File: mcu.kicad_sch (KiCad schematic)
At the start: 33 parts, among them J3 Conn_ARM_SWD_TagConnect_TC203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, J4 Conn_01x02_Pin, U7 RP2040, U9 AT25xxx, Y1 830070868

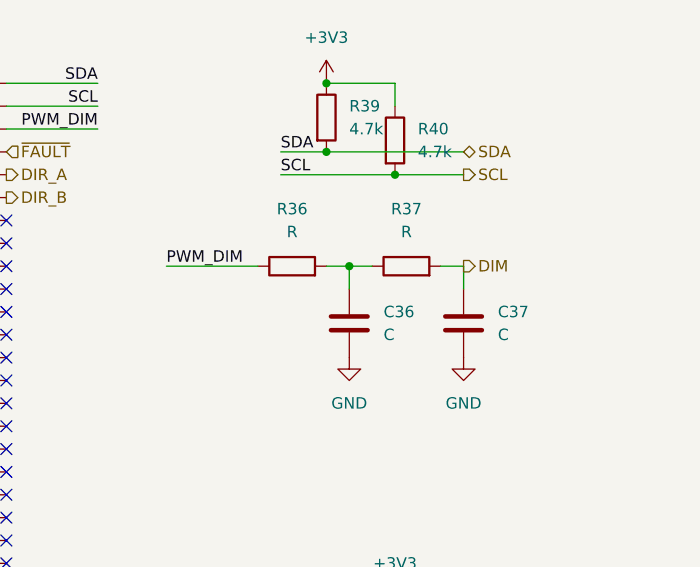
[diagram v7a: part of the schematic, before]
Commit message: Filter values
Updated filter component values from lab experimentation
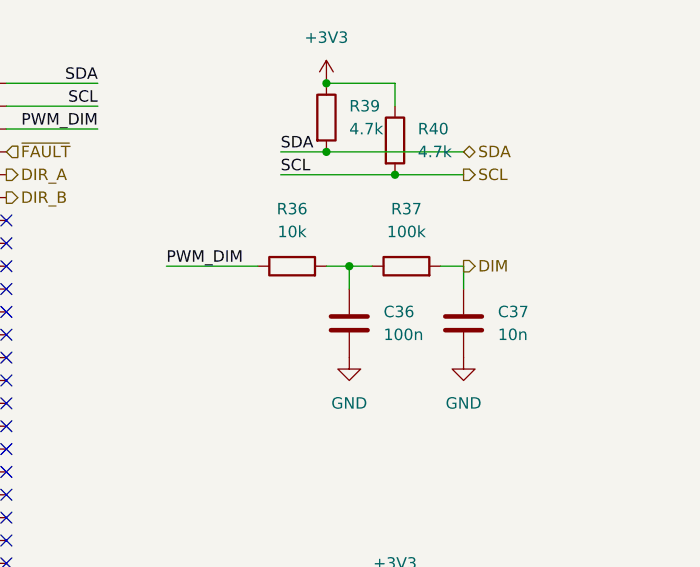
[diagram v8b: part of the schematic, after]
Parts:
- C36: value C -> 100n
- C37: value C -> 10n
- R36: value R -> 10k
- R37: value R -> 100k
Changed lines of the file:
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@@
 			)
 		)
-		(property "Value" "R"
+		(property "Value" "100k"
 			(at 222.25 80.01 90)
 			(effects
@@
 			)
 		)
-		(property "Value" "C"
+		(property "Value" "10n"
 			(at 232.41 91.4399 0)
 			(effects
@@
 			)
 		)
-		(property "Value" "R"
+		(property "Value" "10k"
 			(at 209.55 80.01 90)
 			(effects
@@
 			)
 		)
-		(property "Value" "C"
+		(property "Value" "100n"
 			(at 219.71 91.4399 0)
 			(effects
